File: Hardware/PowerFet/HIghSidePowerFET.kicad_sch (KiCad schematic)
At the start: 23 parts, among them J1 Conn_01x02, U1 TPS4810-Q1, U2 LTV-356T

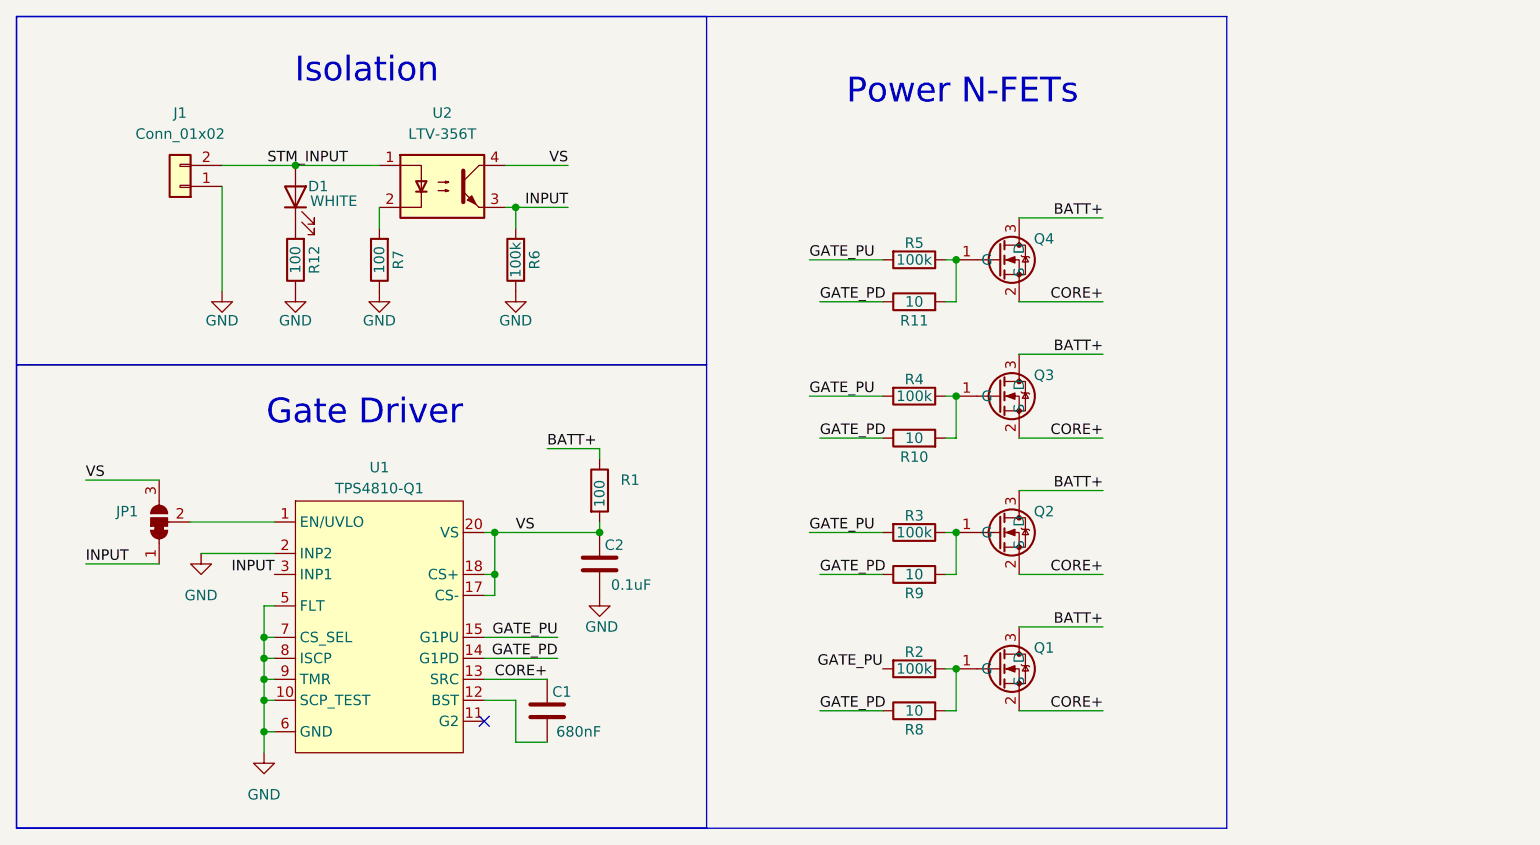
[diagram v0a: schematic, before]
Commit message: BMS updates, power/fet final updates
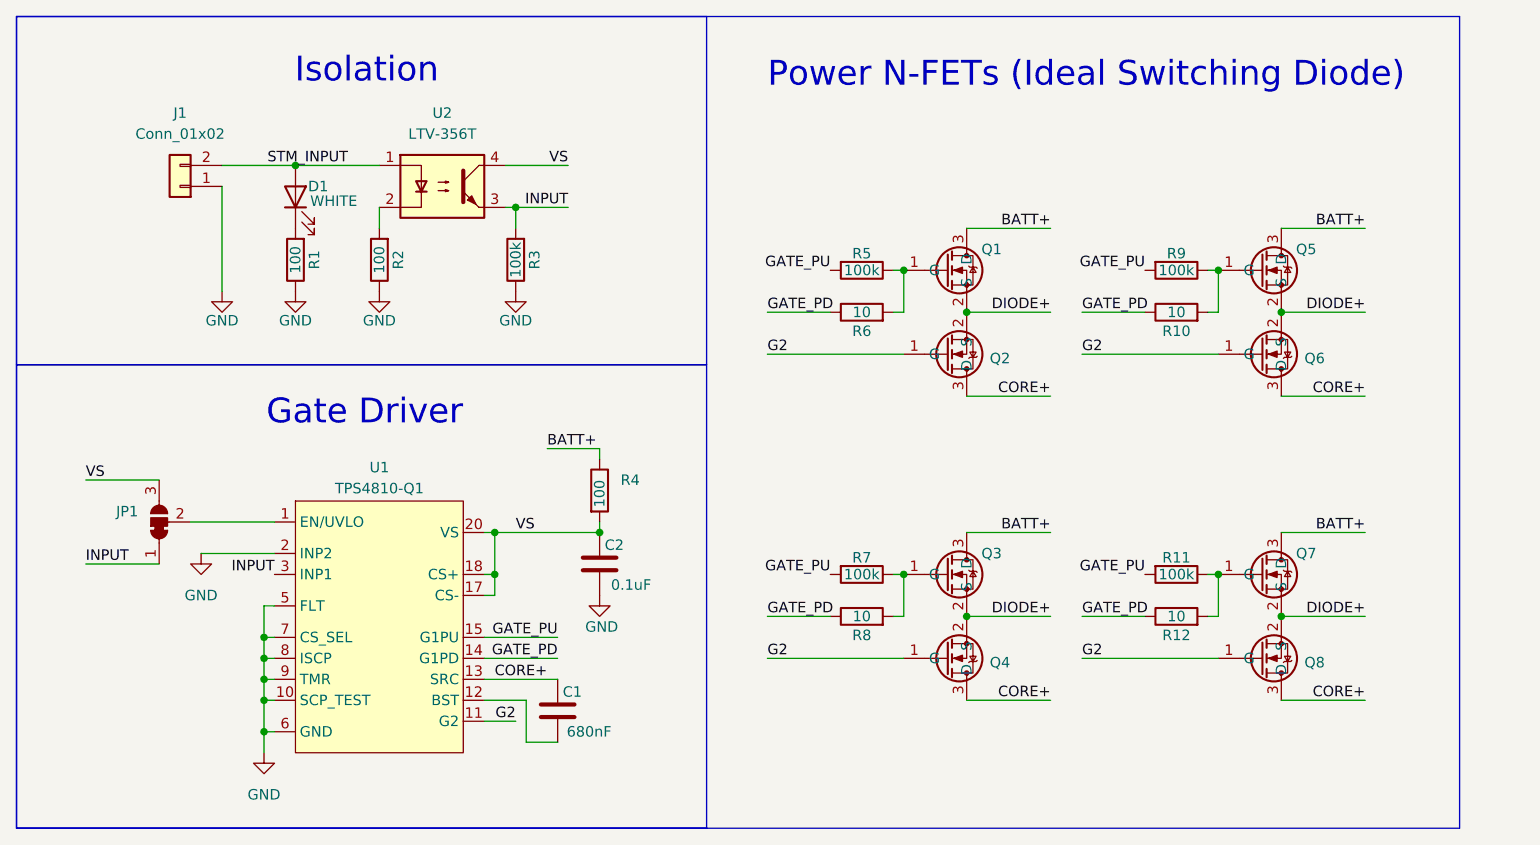
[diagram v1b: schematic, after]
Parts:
- removed Q3: ~, OlinBAD:NTBLS0D8N08X, symbol OlinBAD:T_01_NTBLS0D8N08X
- removed R3, R4: 100k, Resistor_SMD:R_0603_1608Metric, symbol Device:R
- added Q1, Q5, Q6, Q7, Q8: ~, BAD_LIB:NTBLS0D8N08X, symbol OlinBAD:T_01_NTBLS0D8N08X
- added R12, R6: 10, Resistor_SMD:R_0603_1608Metric, symbol Device:R
- Q2, Q4: footprint OlinBAD:NTBLS0D8N08X -> BAD_LIB:NTBLS0D8N08X
- Q3: renamed from Q1; footprint OlinBAD:NTBLS0D8N08X -> BAD_LIB:NTBLS0D8N08X
- R11, R9: value 10 -> 100k
- renumbered R12 to R1, R7 to R2, R6 to R3, R1 to R4, R2 to R7
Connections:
- net BATT+: now also Q1.3 (D), Q5.3 (D), Q7.3 (D); no longer Q2.3 (D), Q4.3 (D)
- net CORE+: now also Q2.3 (D), Q4.3 (D), Q6.3 (D), Q8.3 (D); no longer Q2.2 (S), Q3.2 (S), Q4.2 (S)
- net GATE_PD: now also R12.1, R6.1; no longer R11.1, R9.1
- net GATE_PU: now also R11.2, R9.2
- net G2: now reaches Q2.1 (G)
- net G2: now also Q4.1 (G), U1.11 (G2), Q6.1 (G), Q8.1 (G); no longer R9.2
- net at R10.2: now also R9.1, Q5.1 (G)
- new net: Q1.1 (G), R5.1, R6.2
- new net: Q7.1 (G), R11.1, R12.2
- new net DIODE+: Q1.2 (S), Q2.2 (S), Q3.2 (S), Q4.2 (S), Q5.2 (S), Q6.2 (S), Q7.2 (S), Q8.2 (S)
- no-connect marks 1 -> 0
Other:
- note added: "Power N-FETs (Ideal Switching Diode)"
- note removed: "Power N-FETs"
- moved on the sheet: C1, Q3, R7, R8
